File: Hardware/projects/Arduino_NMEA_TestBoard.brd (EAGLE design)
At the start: 104.2 x 56 mm, 27 parts, among them U1 MCP2562-TH

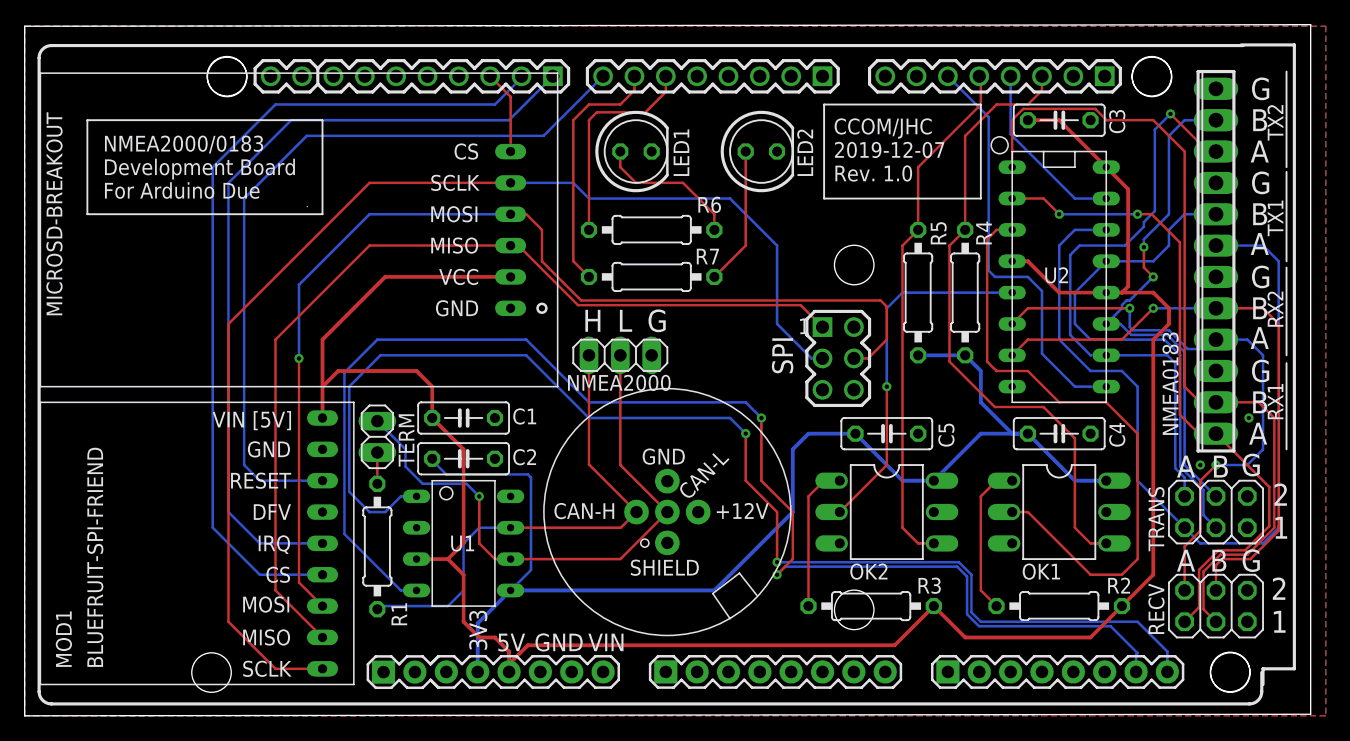
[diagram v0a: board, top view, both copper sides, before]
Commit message: Update to trace layout on Arduino Due development board to smooth out some kinks.
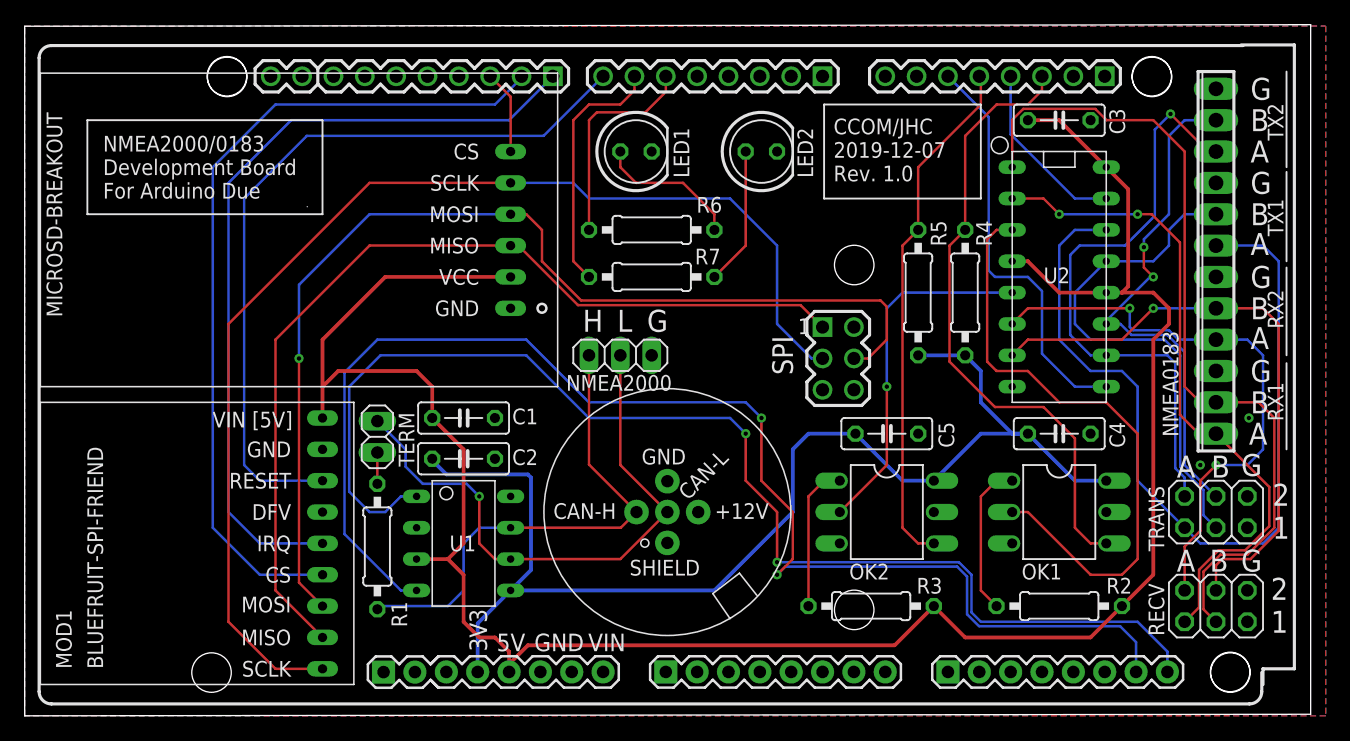
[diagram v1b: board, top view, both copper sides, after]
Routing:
- net N$22: track 47.1 -> 46.5 mm
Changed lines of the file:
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@@
 <drawing>
 <settings>
-<setting alwaysvectorfont="yes"/>
+<setting alwaysvectorfont="no"/>
 <setting verticaltext="up"/>
 </settings>
@@
 <wire x1="45.72" y1="25.4" x2="58.42" y2="25.4" width="0.2032" layer="16"/>
 <via x="59.69" y="24.13" extent="1-16" drill="0.35"/>
-<wire x1="90.043" y1="3.556" x2="90.043" y2="4.953" width="0.2032" layer="16"/>
-<wire x1="90.043" y1="4.953" x2="90.17" y2="5.08" width="0.2032" layer="16"/>
-<wire x1="90.17" y1="5.08" x2="87.9856" y2="7.2644" width="0.2032" layer="16"/>
-<wire x1="87.9856" y1="7.2644" x2="77.3227" y2="7.2644" width="0.2032" layer="16"/>
+<wire x1="90.043" y1="3.556" x2="90.043" y2="5.969" width="0.2032" layer="16"/>
+<wire x1="90.043" y1="5.969" x2="88.7476" y2="7.2644" width="0.2032" layer="16"/>
+<wire x1="88.7476" y1="7.2644" x2="77.3227" y2="7.2644" width="0.2032" layer="16"/>
 <wire x1="77.3227" y1="7.2644" x2="76.3524" y2="8.2347" width="0.2032" layer="16"/>
 <wire x1="76.3524" y1="8.2347" x2="76.3524" y2="11.2827" width="0.2032" layer="16"/>
@@
 <contactref element="C4" pad="1"/>
 <contactref element="C5" pad="1"/>
-<wire x1="41.021" y1="11.811" x2="41.021" y2="19.304" width="0.2032" layer="16"/>
-<wire x1="41.021" y1="19.304" x2="40.767" y2="19.558" width="0.2032" layer="16"/>
-<wire x1="40.767" y1="19.558" x2="34.163" y2="19.558" width="0.2032" layer="16"/>
-<wire x1="34.163" y1="19.558" x2="33.02" y2="20.701" width="0.2032" layer="16"/>
+<wire x1="41.021" y1="11.811" x2="41.021" y2="19.304" width="0.3048" layer="16"/>
+<wire x1="41.021" y1="19.304" x2="40.767" y2="19.558" width="0.3048" layer="16"/>
+<wire x1="40.767" y1="19.558" x2="34.163" y2="19.558" width="0.3048" layer="16"/>
+<wire x1="34.163" y1="19.558" x2="33.02" y2="20.701" width="0.3048" layer="16"/>
 <wire x1="33.02" y1="20.701" x2="33.02" y2="20.828" width="0.2032" layer="16"/>
-<wire x1="39.37" y1="10.16" x2="41.021" y2="11.811" width="0.2032" layer="16"/>
+<wire x1="39.37" y1="10.16" x2="41.021" y2="11.811" width="0.3048" layer="16"/>
 <wire x1="36.703" y1="3.556" x2="36.703" y2="7.493" width="0.3048" layer="16"/>
 <wire x1="36.703" y1="7.493" x2="39.37" y2="10.16" width="0.3048" layer="16"/>
@@
 <contactref element="U2" pad="6"/>
 <contactref element="NMEA0183" pad="4"/>
-<wire x1="96.52" y1="30.48" x2="95.758" y2="29.718" width="0.2032" layer="16"/>
-<wire x1="95.758" y1="29.718" x2="94.234" y2="29.718" width="0.2032" layer="16"/>
-<wire x1="94.234" y1="29.718" x2="92.71" y2="31.242" width="0.2032" layer="16"/>
+<wire x1="96.52" y1="30.48" x2="93.472" y2="30.48" width="0.2032" layer="16"/>
+<wire x1="93.472" y1="30.48" x2="92.71" y2="31.242" width="0.2032" layer="16"/>
 <wire x1="92.71" y1="31.242" x2="89.789" y2="31.242" width="0.2032" layer="16"/>
 <wire x1="89.789" y1="31.242" x2="89.535" y2="31.496" width="0.2032" layer="16"/>
@@
 <wire x1="84.709" y1="37.338" x2="85.471" y2="38.1" width="0.2032" layer="16"/>
 <wire x1="85.471" y1="38.1" x2="89.154" y2="38.1" width="0.2032" layer="16"/>
-<wire x1="89.154" y1="38.1" x2="90.678" y2="39.624" width="0.2032" layer="16"/>
-<wire x1="90.678" y1="39.624" x2="90.678" y2="40.005" width="0.2032" layer="16"/>
-<wire x1="91.567" y1="40.894" x2="90.678" y2="40.005" width="0.2032" layer="16"/>
+<wire x1="91.567" y1="40.513" x2="89.154" y2="38.1" width="0.2032" layer="16"/>
 <wire x1="92.837" y1="48.768" x2="91.567" y2="47.498" width="0.2032" layer="16"/>
-<wire x1="91.567" y1="47.498" x2="91.567" y2="40.894" width="0.2032" layer="16"/>
+<wire x1="91.567" y1="47.498" x2="91.567" y2="40.513" width="0.2032" layer="16"/>
 </signal>
 <signal name="N$28">
@@
 <wire x1="90.678" y1="36.322" x2="91.44" y2="35.56" width="0.2032" layer="1"/>
 <via x="91.44" y="35.56" extent="1-16" drill="0.35"/>
-<wire x1="89.5322" y1="33.6522" x2="89.27313125" y2="33.6522" width="0.2032" layer="16"/>
-<wire x1="89.27313125" y1="33.6522" x2="88.9028" y2="33.28186875" width="0.2032" layer="16"/>
-<wire x1="88.9028" y1="33.28186875" x2="88.9028" y2="33.0228" width="0.2032" layer="16"/>
-<wire x1="88.9028" y1="33.0228" x2="87.63" y2="31.75" width="0.2032" layer="16"/>
-<wire x1="91.44" y1="35.56" x2="89.5322" y2="33.6522" width="0.2032" layer="16"/>
+<wire x1="87.63" y1="32.00906875" x2="87.63" y2="31.75" width="0.2032" layer="16"/>
+<wire x1="91.44" y1="35.56" x2="91.18093125" y2="35.56" width="0.2032" layer="16"/>
+<wire x1="91.18093125" y1="35.56" x2="87.63" y2="32.00906875" width="0.2032" layer="16"/>
 </signal>
 <signal name="N$24">
